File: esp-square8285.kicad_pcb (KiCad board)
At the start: 2 copper layers, 21.3 x 26.4 mm, 13 parts

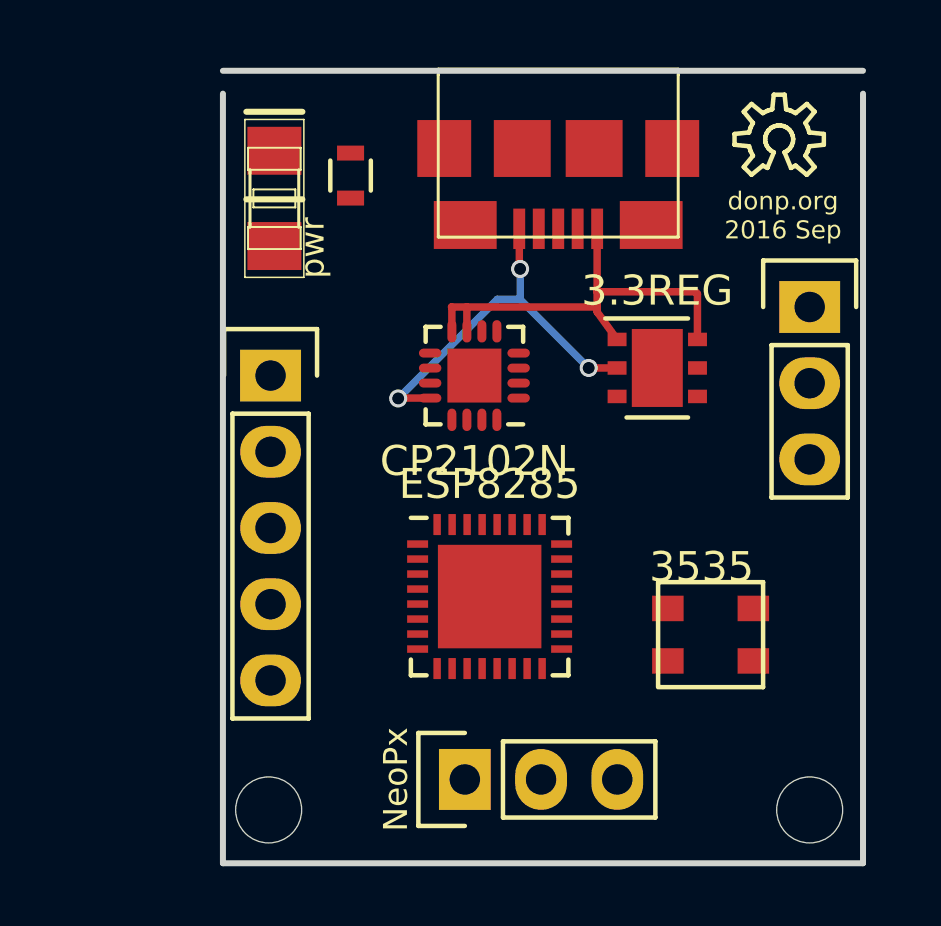
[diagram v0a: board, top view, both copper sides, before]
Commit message: use JST connector
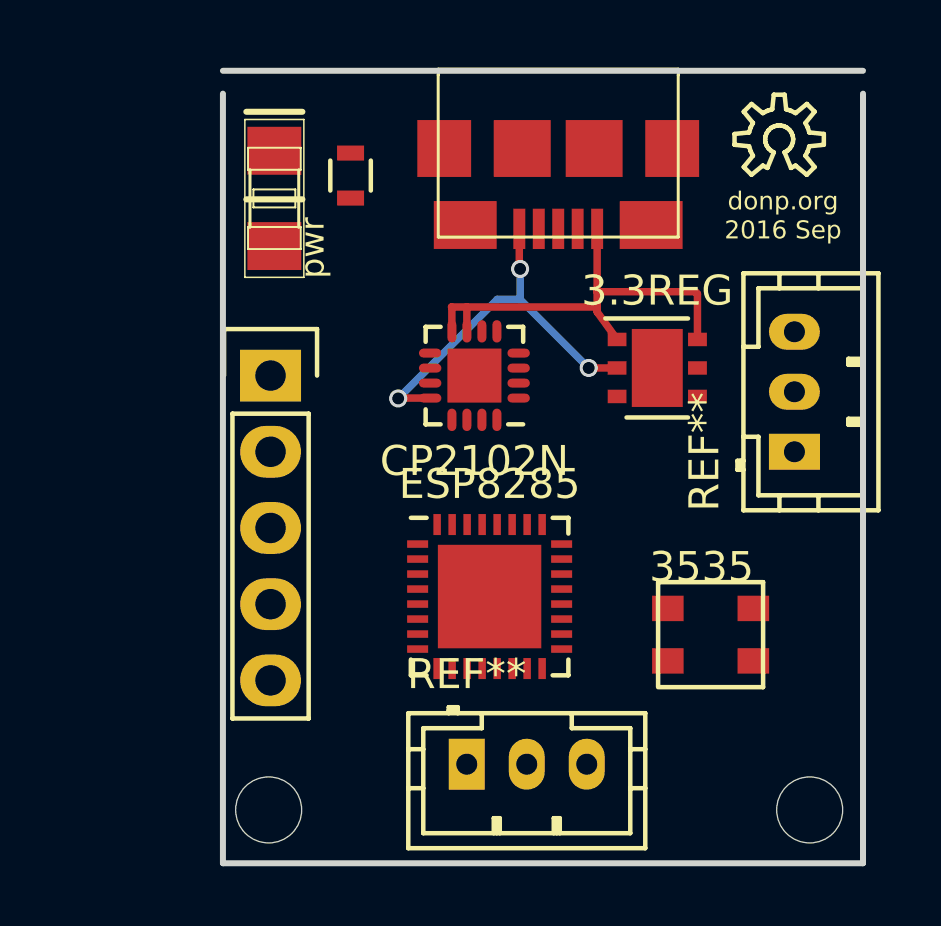
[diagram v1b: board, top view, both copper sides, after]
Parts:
- removed the ? at (151.6, 45.5)
- removed NeoPx: Pin_Header_Straight_1x03, Pin_Headers:Pin_Header_Straight_1x03
- added REF**: JST_PH_B3B-PH-K_03x2.00mm_Straight, Connectors_JST:JST_PH_B3B-PH-K_03x2.00mm_Straight, F.Cu at (151.1, 50.3)
- added REF**: JST_PH_B3B-PH-K_03x2.00mm_Straight, Connectors_JST:JST_PH_B3B-PH-K_03x2.00mm_Straight, F.Cu at (140.2, 60.7)

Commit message: add some traces, use QFN20
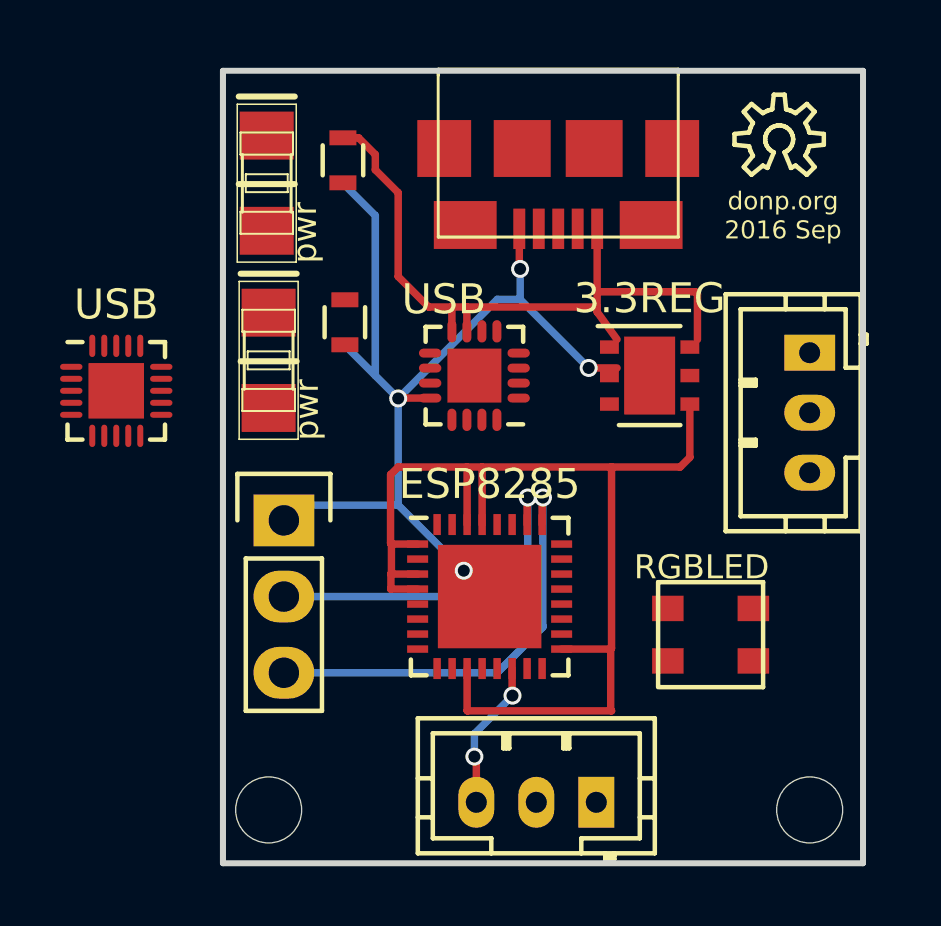
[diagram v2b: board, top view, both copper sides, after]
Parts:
- removed the ? at (133.7, 47.8)
- added ?: R_0603, Resistors_SMD:R_0603, F.Cu at (136.1, 46.0)
- added ?: Pin_Header_Straight_1x03, Pin_Headers:Pin_Header_Straight_1x03, F.Cu at (134.1, 52.6)
- added USB: UQFN-20-1EP_3x3mm_Pitch0.4mm, Housings_DFN_QFN:UQFN-20-1EP_3x3mm_Pitch0.4mm, F.Cu at (128.5, 48.3)
- added pwr: >VALUE, aalay:aalay-LED1206, F.Cu at (133.5, 41.3)
- moved pwr 5.40 mm to (133.6, 47.2)
- moved ? 4.50 mm to (144.5, 62.0), turned to 180 degrees
- moved ? 3.34 mm to (151.6, 47.0), turned to 270 degrees
- moved ? 0.57 mm to (136.1, 40.6)
- moved 3.3REG 0.36 mm to (146.3, 47.8)
- renumbered REF** to ?, 3535 to RGBLED, CP2102N to USB
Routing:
- net (no net): track 28.3 -> 126.1 mm, vias 3 -> 8
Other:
- outline, holes or cut-outs redrawn

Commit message: mostly there
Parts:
- removed the USB at (128.5, 48.3)
- added GPIO0: Measurement_Point_Round-SMD-Pad_Small, Measurement_Points:Measurement_Point_Round-SMD-Pad_Small, F.Cu at (136.9, 59.1)
- moved ? 3.21 mm to (150.6, 50.0), turned to 90 degrees
- moved USB 0.51 mm to (140.5, 48.3), turned to 0 degrees
- moved ? 0.25 mm to (143.3, 38.5)
- gave numbers to parts that had none: 1
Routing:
- net (no net): track 126.1 -> 261.7 mm, vias 8 -> 23
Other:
- board text added: "GND"
- board text added: "RX"
- board text added: "TX"

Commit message: real progress
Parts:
- added OLED: SSD1306, oled:SSD1306, B.Cu at (149.5, 55.9)
- ?: value JST_PH_B3B-PH-K_03x2.00mm_Straight -> JST_PH_03x2.00mm
- ESP8285: value QFN-32-1EP_5x5mm_Pitch0.5mm -> QFN-32-5x5
- GPIO0: value Measurement_Point_Round-SMD-Pad_Small -> Measure
- SERIAL: value Pin_Header_Straight_1x03 -> Pin 1x03
- USB: value QFN-16-1EP_3x3mm_Pitch0.5mm -> QFN-16-3x3
- moved RGBLED 1.08 mm to (147.6, 55.6)
- renumbered pwr to wifi
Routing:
- net (no net): track 261.7 -> 336.3 mm, vias 23 -> 33

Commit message: segment cleanup
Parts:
- ? (x2): value MountingHole_2.2mm_M2 -> Hole_M2
- moved ? 0.25 mm to (150.6, 49.8)
- moved OLED 0.13 mm to (149.4, 55.9)
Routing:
- net (no net): track 336.3 -> 321.1 mm, vias 33 -> 32
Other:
- board text added: "donp.org 2016 Oct"
- board text removed: "donp.org 2016 Sep"

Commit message: esp8285 2016-Nov
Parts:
- removed pwr, wifi: >VALUE, aalay:aalay-LED1206
- added ?: LED_1206, LEDs:LED_1206, F.Cu at (133.7, 46.9)
- added ?: LED_1206, LEDs:LED_1206, F.Cu at (133.7, 41.2)
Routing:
- net (no net): track 321.1 -> 320.1 mm
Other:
- board text added: "donp.org 2016 Nov"
- board text removed: "donp.org 2016 Oct"

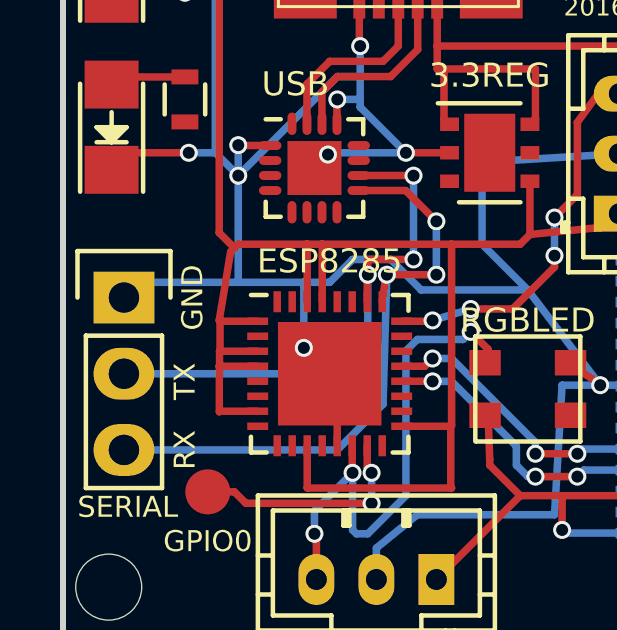
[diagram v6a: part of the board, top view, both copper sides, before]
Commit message: antenna trace
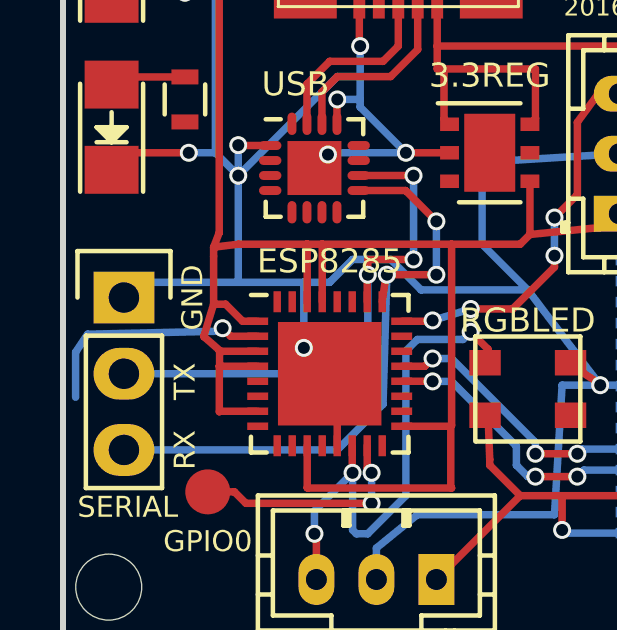
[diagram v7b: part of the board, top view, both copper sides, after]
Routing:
- net (no net): track 320.1 -> 329.3 mm, vias 32 -> 33
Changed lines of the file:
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@@
     (thickness 1.6)
     (drawings 9)
-    (tracks 245)
+    (tracks 256)
     (zones 0)
     (modules 17)
@@
     (effects (font (size 0.6 0.6) (thickness 0.1)))
   )
+  (segment (start 138.57 53.868) (end 137.668 53.868) (width 0.25) (layer F.Cu) (net 0) (status 400000))
+  (segment (start 137.668 53.868) (end 137.4 53.6) (width 0.25) (layer F.Cu) (net 0))
+  (segment (start 132.5 54.4) (end 132.5 55.9) (width 0.25) (layer B.Cu) (net 0))
+  (segment (start 132.9 53.8) (end 132.5 54.4) (width 0.25) (layer B.Cu) (net 0))
+  (segment (start 137.3 53.7) (end 132.9 53.8) (width 0.25) (layer B.Cu) (net 0))
+  (segment (start 137.4 53.6) (end 137.3 53.7) (width 0.25) (layer B.Cu) (net 0))
+  (via (at 137.4 53.6) (size 0.6) (drill 0.4) (layers F.Cu B.Cu) (net 0))
+  (segment (start 137.468 53.668) (end 137.4 53.6) (width 0.25) (layer F.Cu) (net 0))
+  (segment (start 138.57 53.368) (end 138.068 53.368) (width 0.25) (layer F.Cu) (net 0) (status 10))
+  (segment (start 137.5 52.8) (end 137.1 52.8) (width 0.25) (layer F.Cu) (net 0))
+  (segment (start 138.068 53.368) (end 137.5 52.8) (width 0.25) (layer F.Cu) (net 0))
   (segment (start 140.1075 54.2555) (end 141.8325 54.2555) (width 0.25) (layer F.Cu) (net 0) (status 30))
   (segment (start 140.1075 54.2555) (end 140.1075 52.07) (width 0.25) (layer B.Cu) (net 0))
@@
   (segment (start 137.287 42.3) (end 137.054 42.3) (width 0.25) (layer F.Cu) (net 0))
   (segment (start 137.287 50.419) (end 137.287 42.3) (width 0.25) (layer F.Cu) (net 0))
-  (segment (start 137.795 50.927) (end 137.287 50.419) (width 0.25) (layer F.Cu) (net 0))
+  (segment (start 137.1 50.9) (end 137.287 50.419) (width 0.25) (layer F.Cu) (net 0))
   (segment (start 137.054 42.3) (end 136.0805 41.3265) (width 0.25) (layer F.Cu) (net 0) (status 20))
   (segment (start 137.291 54.868) (end 137.291 56.384) (width 0.25) (layer F.Cu) (net 0))
@@
   (segment (start 137.291 54.868) (end 137.299 54.86) (width 0.25) (layer F.Cu) (net 0))
   (segment (start 138.57 54.368) (end 137.299 54.368) (width 0.25) (layer F.Cu) (net 0) (status 10))
-  (segment (start 137.315 54.352) (end 137.315 53.368) (width 0.25) (layer F.Cu) (net 0))
+  (segment (start 137.315 54.352) (end 136.8 53.9) (width 0.25) (layer F.Cu) (net 0))
   (segment (start 137.299 54.368) (end 137.315 54.352) (width 0.25) (layer F.Cu) (net 0))
-  (segment (start 138.57 53.368) (end 137.315 53.368) (width 0.25) (layer F.Cu) (net 0) (status 10))
   (segment (start 147.644 50.476) (end 147.644 48.702) (width 0.25) (layer F.Cu) (net 0) (status 20))
   (segment (start 147.32 50.8) (end 147.644 50.476) (width 0.25) (layer F.Cu) (net 0))
@@
   (segment (start 140.716 50.8) (end 145.034 50.8) (width 0.25) (layer F.Cu) (net 0))
   (segment (start 145.034 50.8) (end 147.32 50.8) (width 0.25) (layer F.Cu) (net 0))
-  (segment (start 137.668 51.054) (end 137.795 50.927) (width 0.25) (layer F.Cu) (net 0))
-  (segment (start 137.795 50.927) (end 137.922 50.8) (width 0.25) (layer F.Cu) (net 0))
-  (segment (start 137.287 53.34) (end 137.668 51.054) (width 0.25) (layer F.Cu) (net 0))
-  (segment (start 137.315 53.368) (end 137.287 53.34) (width 0.25) (layer F.Cu) (net 0))
+  (segment (start 137.1 51.2) (end 137.1 50.9) (width 0.25) (layer F.Cu) (net 0))
+  (segment (start 137.1 50.9) (end 137.922 50.8) (width 0.25) (layer F.Cu) (net 0))
+  (segment (start 136.772 53.872) (end 137.1 52.8) (width 0.25) (layer F.Cu) (net 0))
+  (segment (start 137.1 52.8) (end 137.1 51.2) (width 0.25) (layer F.Cu) (net 0))
+  (segment (start 136.8 53.9) (end 136.772 53.872) (width 0.25) (layer F.Cu) (net 0))
   (segment (start 141.95806 44.16806) (end 141.95806 42.60596) (width 0.25) (layer F.Cu) (net 0) (status 20))
   (segment (start 141.986 44.196) (end 141.95806 44.16806) (width 0.25) (layer F.Cu) (net 0))

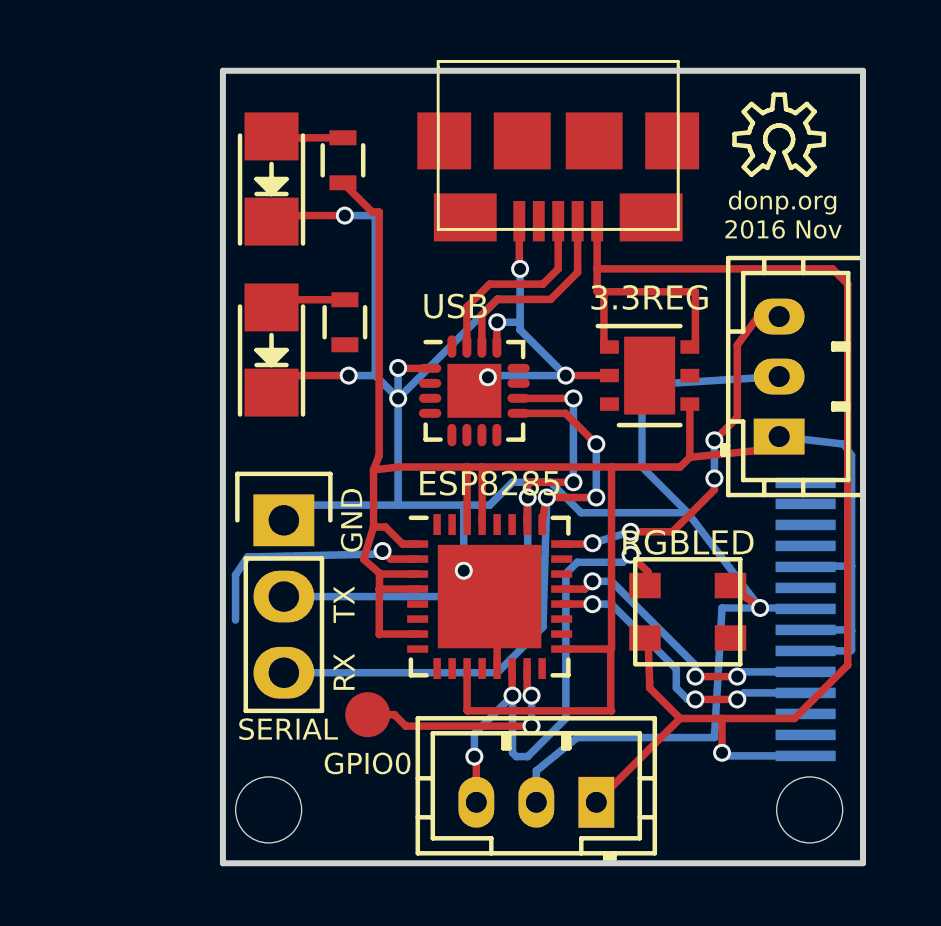
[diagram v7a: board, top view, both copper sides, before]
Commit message: power the usb!
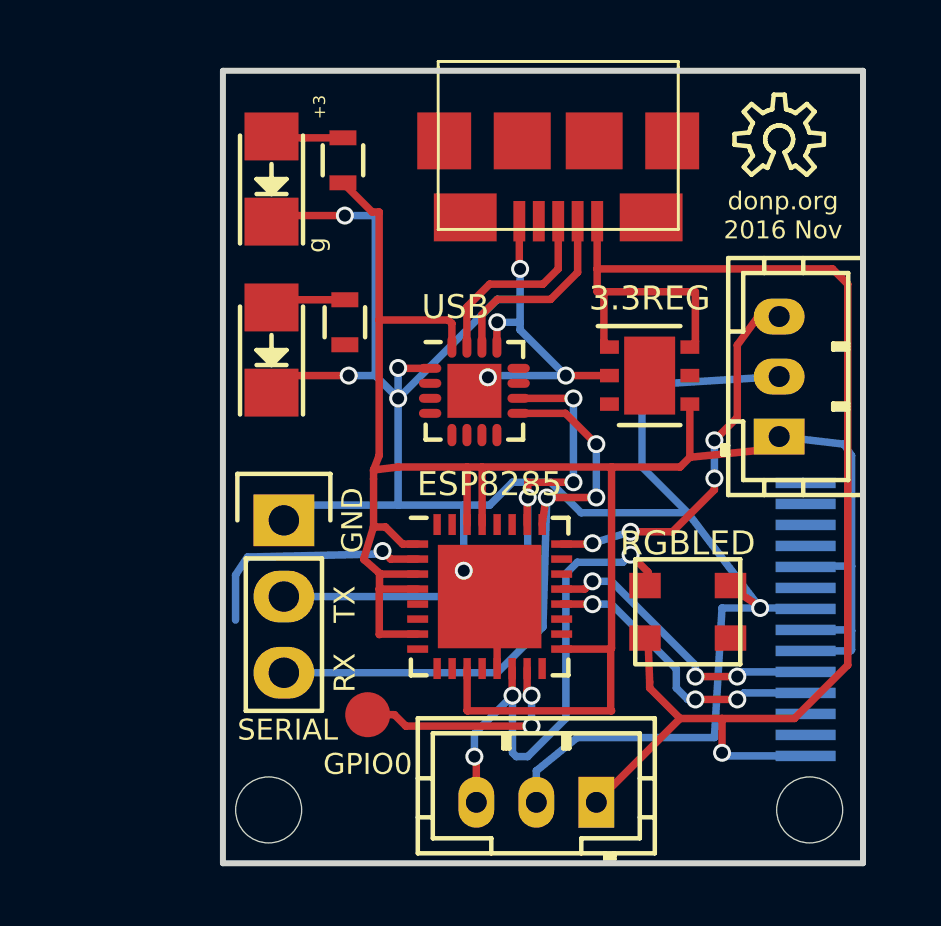
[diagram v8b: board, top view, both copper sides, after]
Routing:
- net (no net): track 329.3 -> 332.6 mm
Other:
- board text added: "+3"
- board text added: "g"
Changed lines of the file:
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@@
     (area 130.308762 32.250666 155.697 66.505)
     (thickness 1.6)
-    (drawings 9)
-    (tracks 256)
+    (drawings 11)
+    (tracks 260)
     (zones 0)
     (modules 17)
@@
     )
   )
+  (gr_text +3 (at 135.3 38.8 90) (layer F.SilkS)
+    (effects (font (size 0.4 0.4) (thickness 0.1)))
+  )
+  (gr_text g (at 135.2 43.4 90) (layer F.SilkS)
+    (effects (font (size 0.6 0.6) (thickness 0.1)))
+  )
   (gr_text TX (at 136.144 55.372 90) (layer F.SilkS)
     (effects (font (size 0.7 0.7) (thickness 0.1)))
@@
     (effects (font (size 0.6 0.6) (thickness 0.1)))
   )
-  (segment (start 138.57 53.868) (end 137.668 53.868) (width 0.25) (layer F.Cu) (net 0) (status 400000))
+  (segment (start 139.712 46.785) (end 139.712 46.012) (width 0.25) (layer F.Cu) (net 0))
+  (segment (start 139.6 45.9) (end 137.287 45.9) (width 0.25) (layer F.Cu) (net 0))
+  (segment (start 139.712 46.012) (end 139.6 45.9) (width 0.25) (layer F.Cu) (net 0))
+  (segment (start 138.57 53.868) (end 137.668 53.868) (width 0.25) (layer F.Cu) (net 0))
   (segment (start 137.668 53.868) (end 137.4 53.6) (width 0.25) (layer F.Cu) (net 0))
   (segment (start 132.5 54.4) (end 132.5 55.9) (width 0.25) (layer B.Cu) (net 0))
@@
   (segment (start 134.26786 47.752) (end 133.7 48.31986) (width 0.25) (layer F.Cu) (net 0) (status 30))
   (segment (start 137.287 42.3) (end 137.054 42.3) (width 0.25) (layer F.Cu) (net 0))
-  (segment (start 137.287 50.419) (end 137.287 42.3) (width 0.25) (layer F.Cu) (net 0))
+  (segment (start 137.287 50.419) (end 137.287 45.9) (width 0.25) (layer F.Cu) (net 0))
+  (segment (start 137.287 45.9) (end 137.287 42.3) (width 0.25) (layer F.Cu) (net 0))
   (segment (start 137.1 50.9) (end 137.287 50.419) (width 0.25) (layer F.Cu) (net 0))
   (segment (start 137.054 42.3) (end 136.0805 41.3265) (width 0.25) (layer F.Cu) (net 0) (status 20))
